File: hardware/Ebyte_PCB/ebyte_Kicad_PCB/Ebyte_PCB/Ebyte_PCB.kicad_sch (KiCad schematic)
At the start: 24 parts, among them U1 DF11, U2 TPS5405DR, U4 Ebyte, U5 CONMMCX001, U6 MIC69303RT

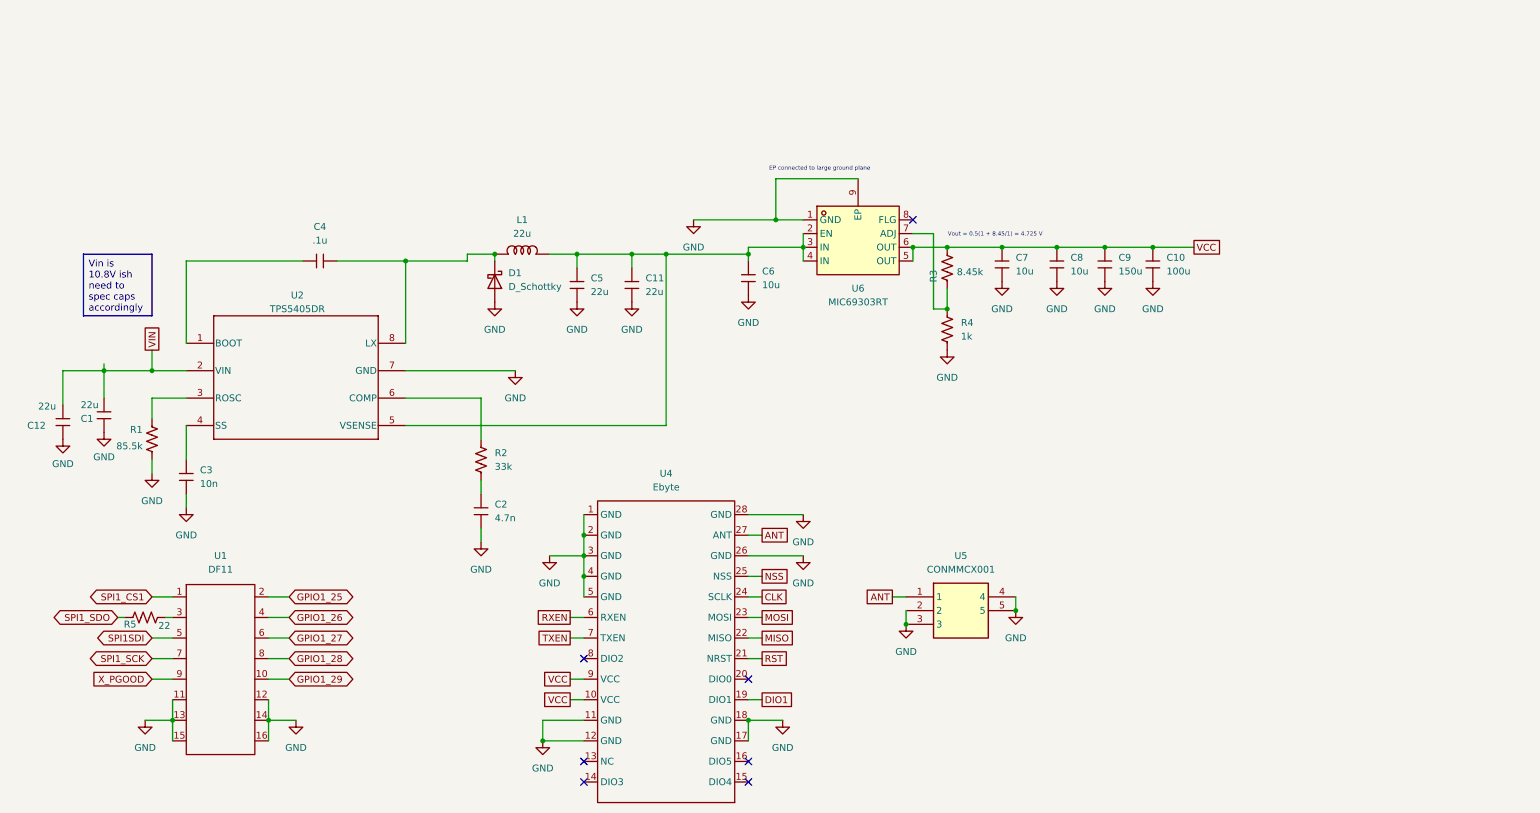
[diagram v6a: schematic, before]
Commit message: updated df11 connectors
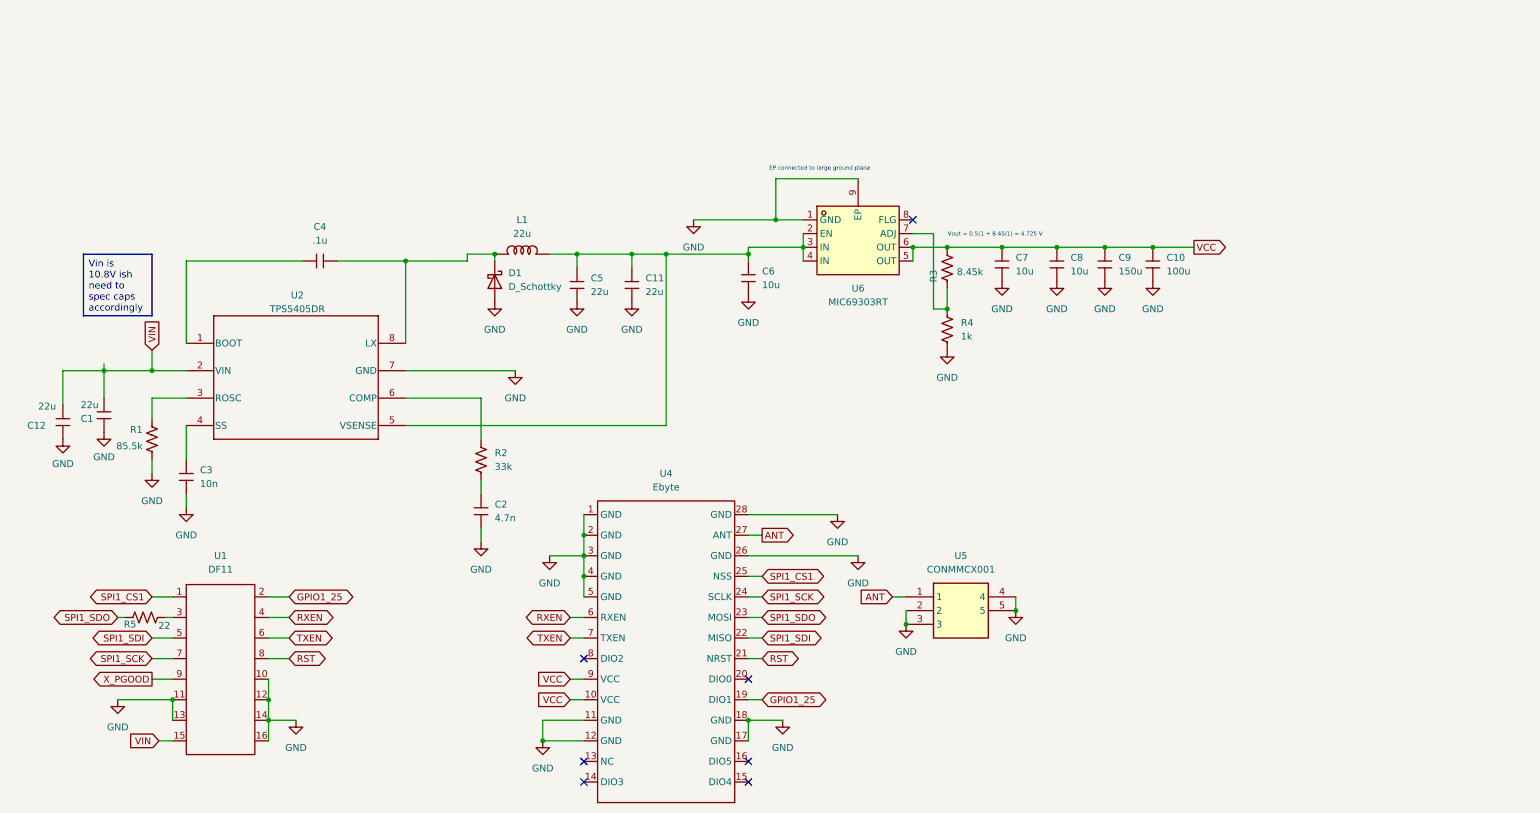
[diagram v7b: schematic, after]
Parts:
- C11, C5: footprint ebyte_footprints:C1206 -> ebyte_footprints:C1210
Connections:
- net CLK is gone; now on net SPI1_SCK: U4.24 (SCLK)
- net DIO1 is gone; now on net GPIO1_25: U4.19 (DIO1)
- net GPIO1_26 is gone; now on net RXEN: U1.4
- net GPIO1_27 is gone; now on net TXEN: U1.6
- net GPIO1_28 is gone; now on net RST: U1.8
- net GPIO1_29 is gone; now on net GND: U1.10
- net MOSI is gone; now on net SPI1_SDO: U4.23 (MOSI)
- net NSS is gone; now on net SPI1_CS1: U4.25 (NSS)
- net SPI1SDI is gone; now on net SPI1_SDI: U1.5
- net GND: no longer U1.15
- net VIN: now also U1.15
- net MISO renamed SPI1_SDI

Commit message: Added Load Switch circuit
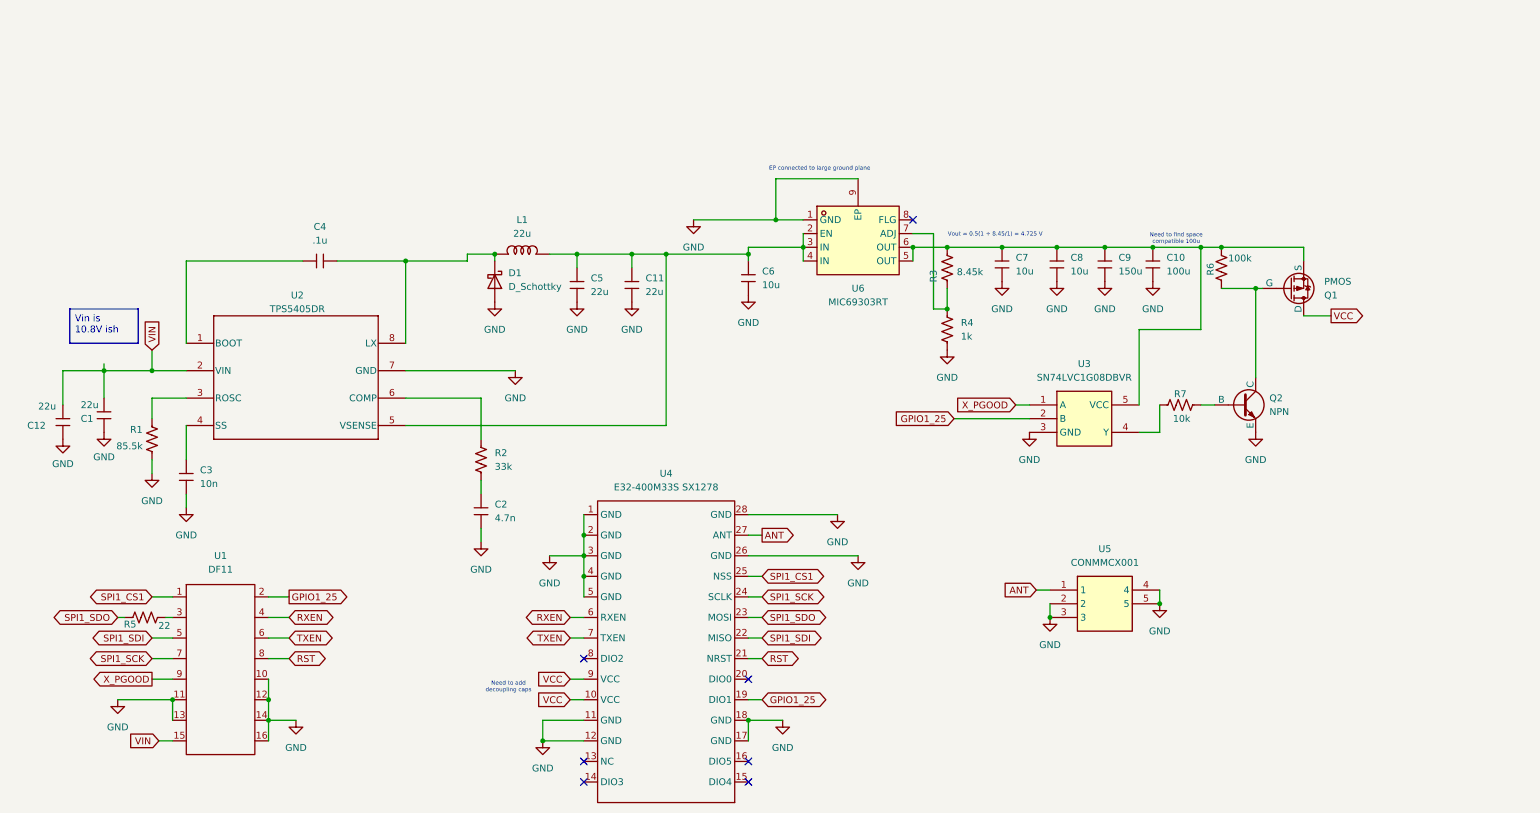
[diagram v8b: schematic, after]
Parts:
- added Q1: PMOS, symbol Simulation_SPICE:PMOS
- added Q2: NPN, symbol Simulation_SPICE:NPN
- added R6: 100k, symbol ebyte__symbols:Resistor
- added R7: 10k, symbol ebyte__symbols:Resistor
- added U3: SN74LVC1G08DBVR, ebyte_footprints:SOT-23-5_L3.0-W1.7-P0.95-LS2.8-BR, symbol ebyte__symbols:SN74LVC1G08DBVR
- U4: value Ebyte -> E32-400M33S SX1278
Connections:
- net GND: now also Q2.3 (E), U3.3 (GND)
- net GPIO1_25: now also U3.2 (B)
- net VCC: now also Q1.1 (D); no longer C10.2, C7.2, C8.2, C9.2, R3.2, U6.5 (OUT), U6.6 (OUT)
- net X_PGOOD: now also U3.1 (A)
- new net: Q1.2 (G), Q2.1 (C), R6.1
- new net: Q2.2 (B), R7.2
- new net: R7.1, U3.4 (Y)
- new net: C10.2, C7.2, C8.2, C9.2, Q1.3 (S), R3.2, R6.2, U3.5 (VCC), U6.5 (OUT), U6.6 (OUT)
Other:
- note added: "Need to add decoupling caps"
- note added: "Need to find space compatible 100u"
- moved on the sheet: U5
